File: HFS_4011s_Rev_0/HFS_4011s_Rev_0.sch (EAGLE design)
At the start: 64 parts, among them IC1 CP2104, J1 2X06, J2 2X12, J3 1X02, J5 1X02, J6 MOLEX_IGRID_15X2CONNECTOR, Q1 mmbt2222, Q2 mmbt2222, Q3 MMUN2133LT1G, Q4 BSS138, Q5 BSS138, SW2 KMR2, U1 TPS61090RSAR, U2 MCP73831T-2ACI/OT, U3 AD5693R, U4 LM3671MF-3.3/NOPB, X2 ESP32_WROOM32_SKINNY

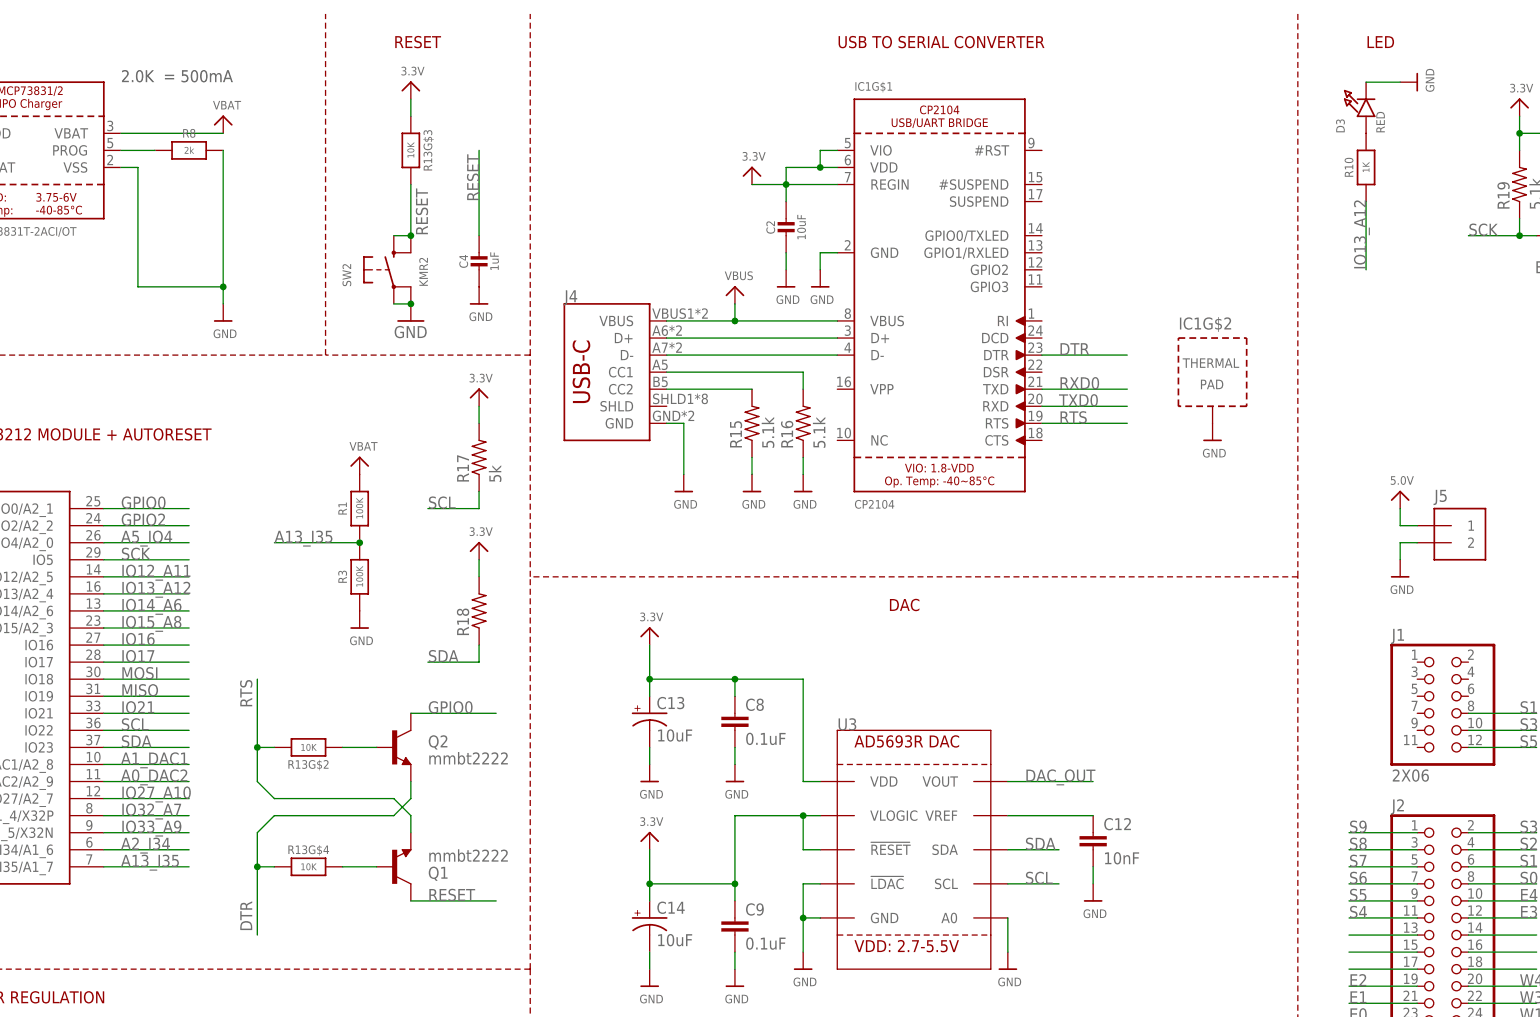
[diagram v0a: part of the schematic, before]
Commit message: Started board layout. Placed battery charge circuitry, usb-serial conversion, and reset components onto board.
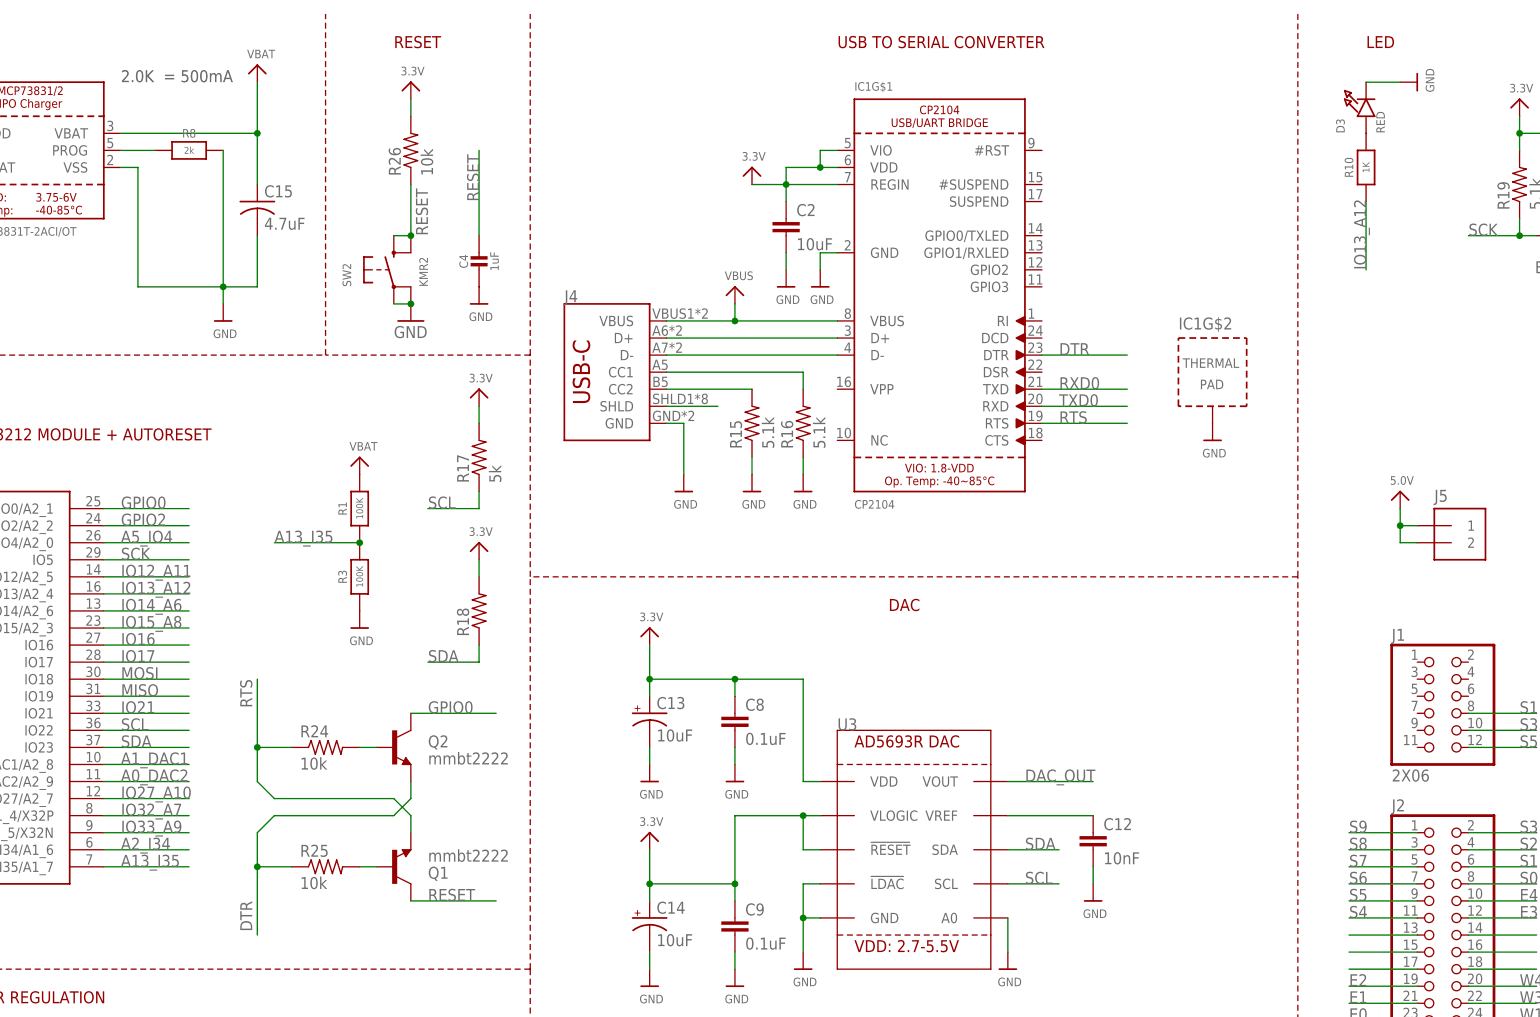
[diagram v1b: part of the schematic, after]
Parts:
- removed R13: 10K, microbuilder:RESISTOR_4PACK
- added C15: 4.7uF, rcl:C-USC1206
- added R24, R25, R26: 10k, rcl:R-US_R0603
- C2: device microbuilder:CAP_CERAMIC0805-NOOUTLINE -> rcl:C-EUC0603
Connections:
- new net SHLD: J4.SHLD
- net 3.3V: now also R26.2; no longer R13G$3.1
- net 5.0V: now also J5.2
- net DTR: now also R25.1; no longer R13G$4.1
- net GND: now also C15.2; no longer J5.2
- net N$12: now also R25.2; no longer R13G$4.2
- net N$13: now also R24.2; no longer R13G$2.1
- net RESET: now also R26.1; no longer R13G$3.2
- net RTS: now also R24.1; no longer R13G$2.2
- net VBAT: now also C15.1

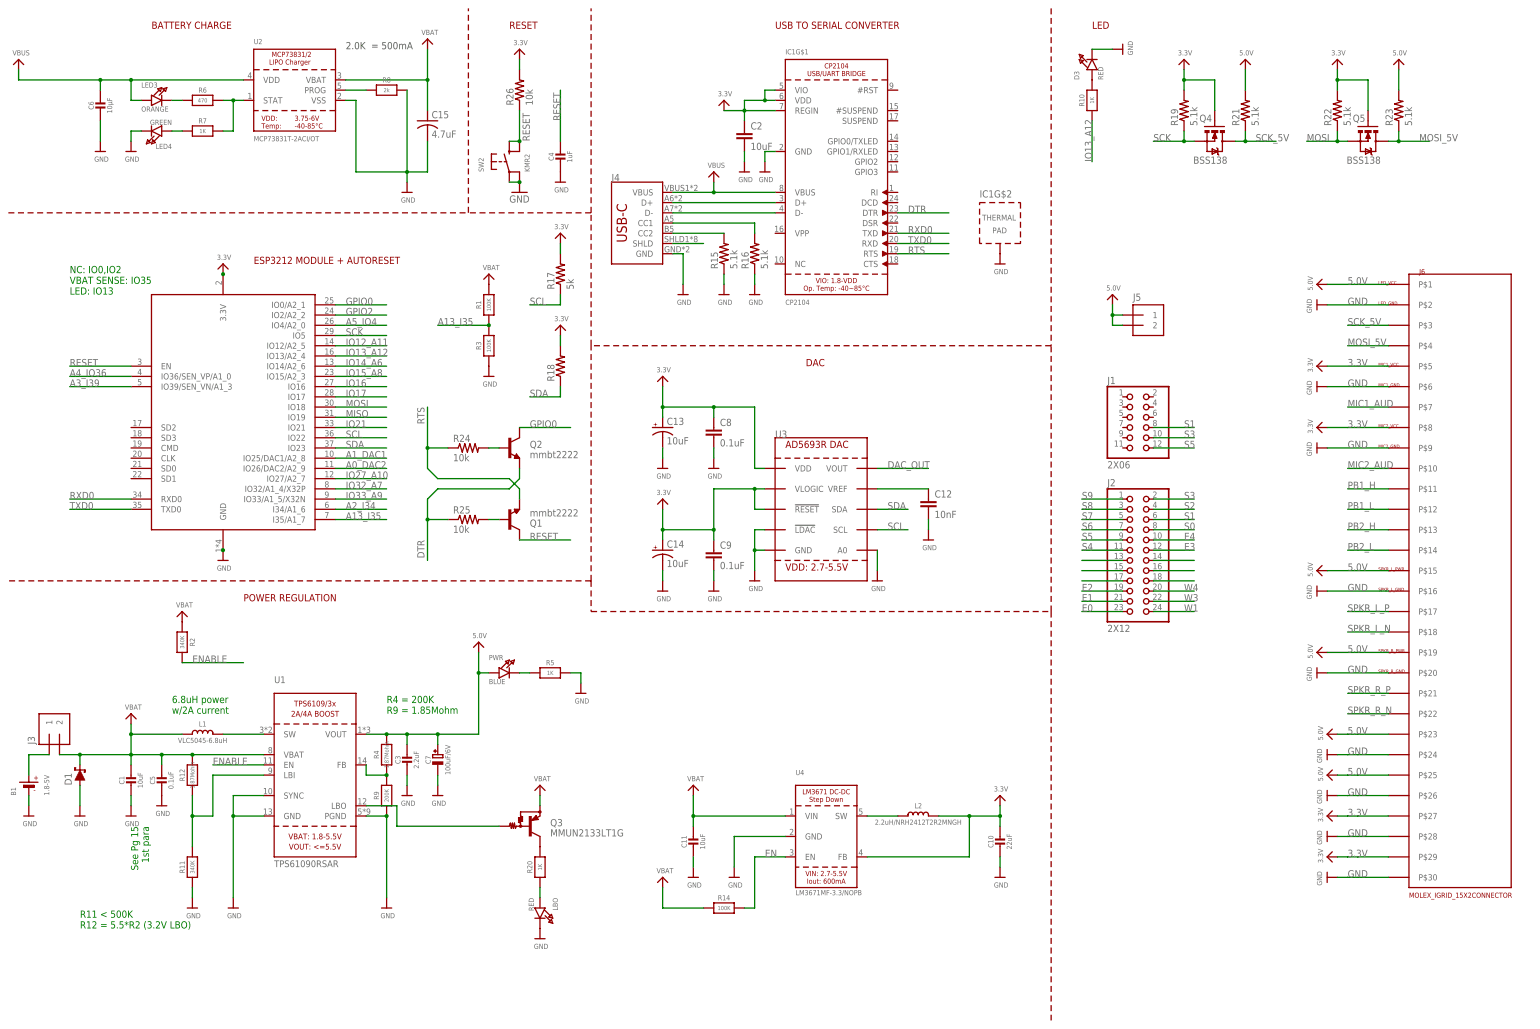
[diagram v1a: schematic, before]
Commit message: Changed usb C back to micro usb. Converted board to a 4-layer design. Routed 5V power supply.
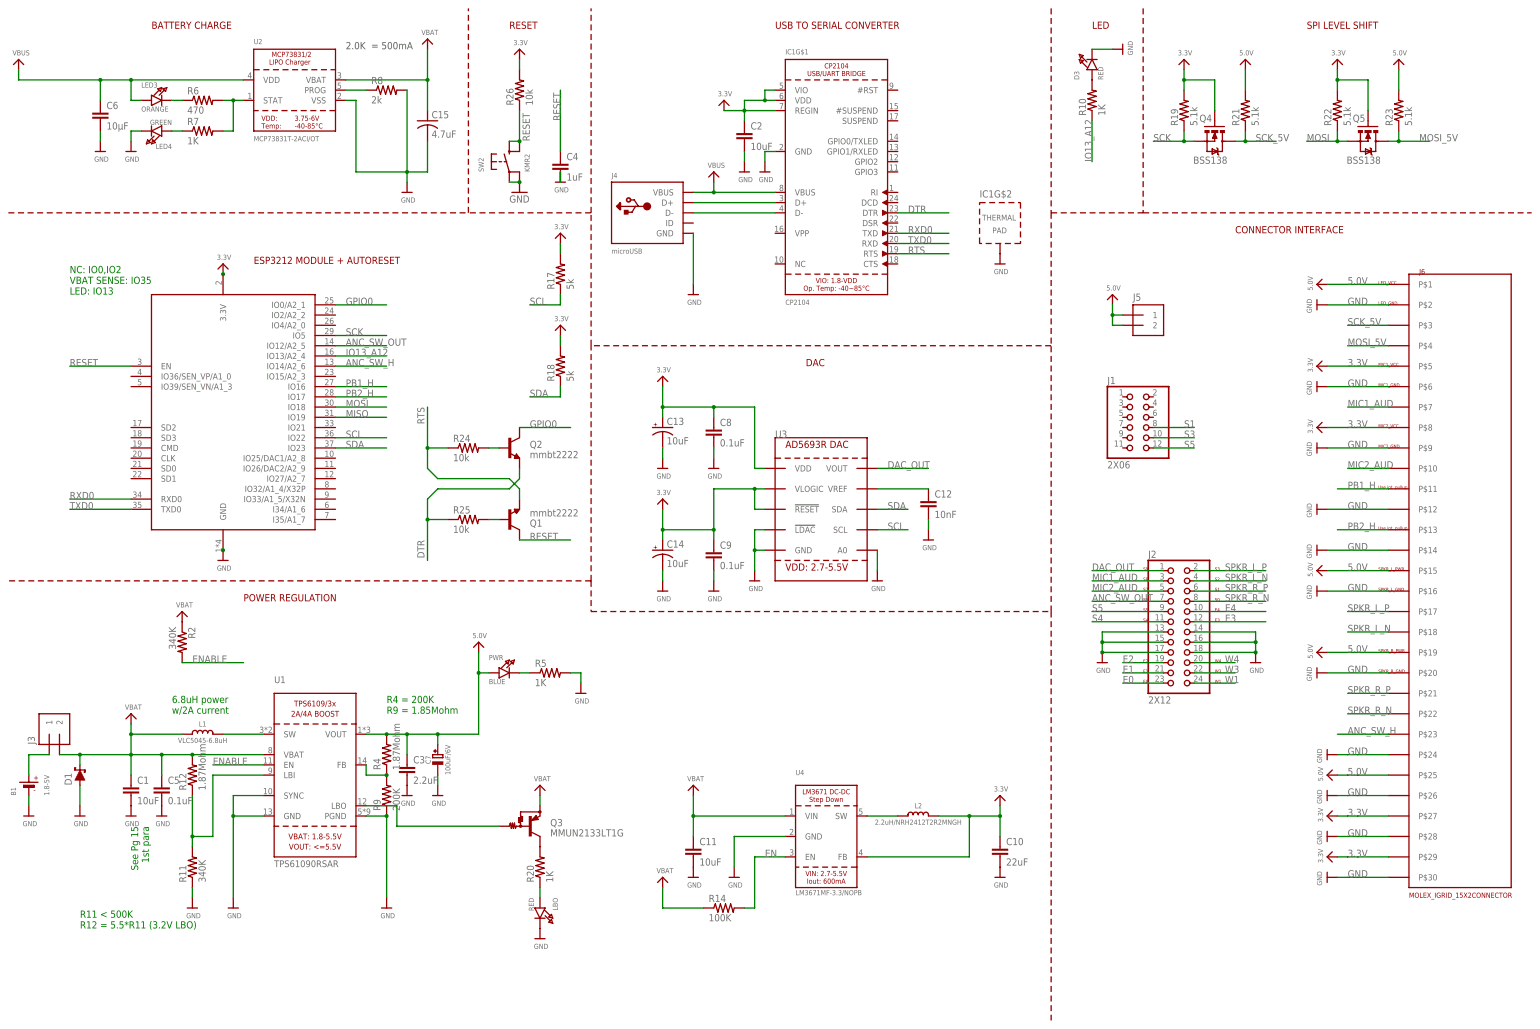
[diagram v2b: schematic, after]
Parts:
- removed R1, R3: 100K, microbuilder:RESISTOR_0603_NOOUT
- removed R15, R16: 5.1k, rcl:R-US_R0603
- C1, C10, C11, C3, C5, C6: device microbuilder:CAP_CERAMIC0805-NOOUTLINE -> rcl:C-EUC0603
- C4: device microbuilder:CAP_CERAMIC0603_NO -> rcl:C-EUC0603
- J4: value (none) -> microUSB; device SparkFun-Connectors:USB_C16PIN -> microbuilder:USBMICRO_20329
- R10: device microbuilder:RESISTOR_0603_NOOUT -> rcl:R-US_R0603
- R11, R12, R14, R2, R20, R4, R5, R6, R7, R8, R9: device microbuilder:RESISTOR0805_NOOUTLINE -> rcl:R-US_R0603
- R18: value (none) -> 5k
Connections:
- removed net A0_DAC2: X2.IO26/DAC2/A2_9
- removed net A13_I35: R1.1, R3.2, X2.I35/A1_7
- removed net A1_DAC1: X2.IO25/DAC1/A2_8
- removed net A2_I34: X2.I34/A1_6
- removed net A3_I39: X2.IO39/SEN_VN/A1_3
- removed net A4_IO36: X2.IO36/SEN_VP/A1_0
- removed net A5_IO4: X2.IO4/A2_0
- removed net GPIO2: X2.IO2/A2_2
- removed net IO12_A11: X2.IO12/A2_5
- removed net IO14_A6: X2.IO14/A2_6
- removed net IO15_A8: X2.IO15/A2_3
- removed net IO16: X2.IO16
- removed net IO17: X2.IO17
- removed net IO21: X2.IO21
- removed net IO27_A10: X2.IO27/A2_7
- removed net IO32_A7: X2.IO32/A1_4/X32P
- removed net IO33_A9: X2.IO33/A1_5/X32N
- removed net N$18: J4.CC1, R16.2
- removed net N$19: J4.CC2, R15.2
- removed net N$27: J2.14
- removed net N$28: J2.16
- removed net N$29: J2.18
- removed net N$39: J2.13
- removed net N$40: J2.15
- removed net N$41: J2.17
- removed net PB1_L: J6.P$12
- removed net PB2_L: J6.P$14
- removed net S0: J2.8
- removed net S2: J2.4
- removed net S6: J2.7
- removed net S7: J2.5
- removed net S8: J2.3
- removed net S9: J2.1
- removed net SHLD: J4.SHLD
- new net ANC_SW_H: J6.P$23, X2.IO14/A2_6
- new net ANC_SW_OUT: J2.7, X2.IO12/A2_5
- net 5.0V: no longer J6.P$23
- net DAC_OUT: now also J2.1
- net GND: now also J2.13, J2.14, J2.15, J2.16, J2.17, J2.18, J6.P$12, J6.P$14; no longer R15.1, R16.1, R3.1
- net MIC1_AUD: now also J2.3
- net MIC2_AUD: now also J2.5
- net PB1_H: now also X2.IO16
- net PB2_H: now also X2.IO17
- net S1: no longer J2.6
- net S3: no longer J2.2
- net SPKR_L_N: now also J2.4
- net SPKR_L_P: now also J2.2
- net SPKR_R_N: now also J2.8
- net SPKR_R_P: now also J2.6
- net VBAT: no longer R1.2
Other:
- note added: "CONNECTOR INTERFACE"
- note added: "E0"
- note added: "E1"
- note added: "E2"
- note added: "E3"
- note added: "E4"
- note added: "R11 < 500K R12 = 5.5*R11 (3.2V LBO)"
- note added: "S0"
- note added: "S1"
- note added: "S2"
- note added: "S3"
- note added: "S4"
- note added: "S5"
- note added: "S6"
- note added: "S7"
- note added: "S8"
- note added: "S9"
- note added: "SPI LEVEL SHIFT"
- note added: "Use int. pullup"
- note added: "W1"
- note added: "W3"
- note added: "W4"
- note removed: "R11 < 500K R12 = 5.5*R2 (3.2V LBO)"
- moved on the sheet: C1, C10, C11, C3, C4, C5, C6, J2

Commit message: Routed all components (0 airwire errors). But getting a lot of clearance errors. Also changed connector pinout
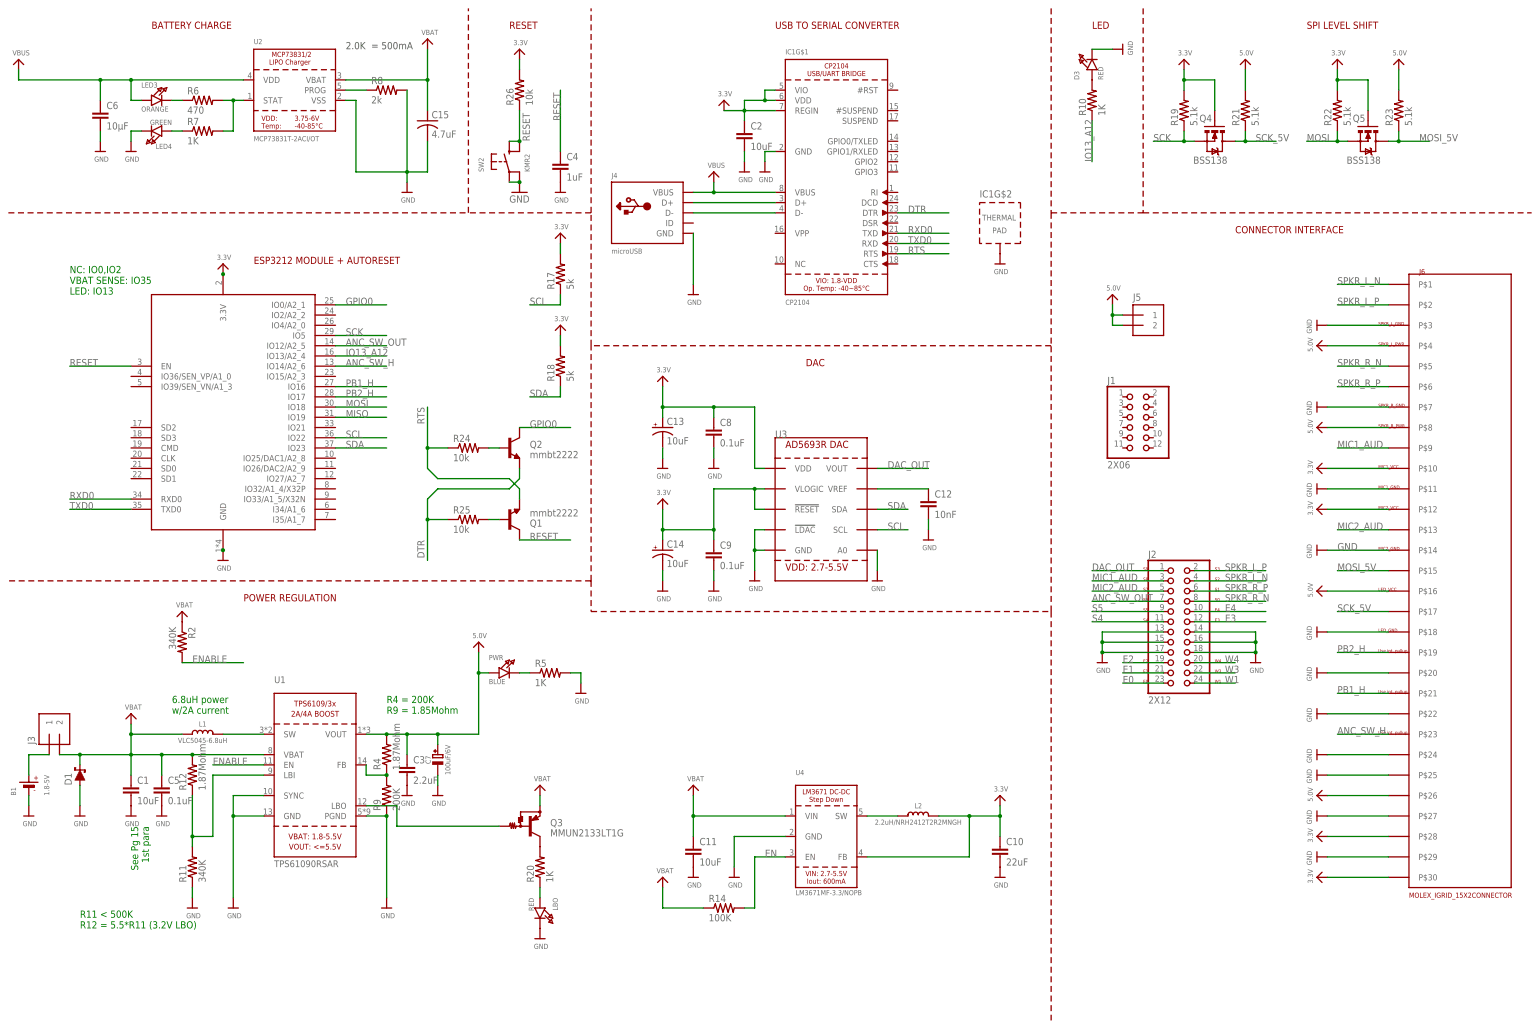
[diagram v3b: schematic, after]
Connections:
- removed net S1: J1.8
- removed net S3: J1.10
- net 3.3V: now also J6.P$10, J6.P$12, J6.P$28, J6.P$30; no longer J6.P$27, J6.P$29, J6.P$5, J6.P$8
- net 5.0V: now also J6.P$16, J6.P$26, J6.P$4, J6.P$8; no longer J6.P$1, J6.P$15, J6.P$19, J6.P$25
- net GND: now also J6.P$11, J6.P$18, J6.P$22, J6.P$25, J6.P$27, J6.P$29, J6.P$3, J6.P$7; no longer J6.P$12, J6.P$16, J6.P$2, J6.P$26, J6.P$28, J6.P$30, J6.P$6, J6.P$9
- net MIC1_AUD: now also J6.P$9; no longer J6.P$7
- net MIC2_AUD: now also J6.P$13; no longer J6.P$10
- net MOSI_5V: now also J6.P$15; no longer J6.P$4
- net PB1_H: now also J6.P$21; no longer J6.P$11
- net PB2_H: now also J6.P$19; no longer J6.P$13
- net S5: no longer J1.12
- net SCK_5V: now also J6.P$17; no longer J6.P$3
- net SPKR_L_N: now also J6.P$1; no longer J6.P$18
- net SPKR_L_P: now also J6.P$2; no longer J6.P$17
- net SPKR_R_N: now also J6.P$5; no longer J6.P$22
- net SPKR_R_P: now also J6.P$6; no longer J6.P$21
